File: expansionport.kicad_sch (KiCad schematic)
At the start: 23 parts

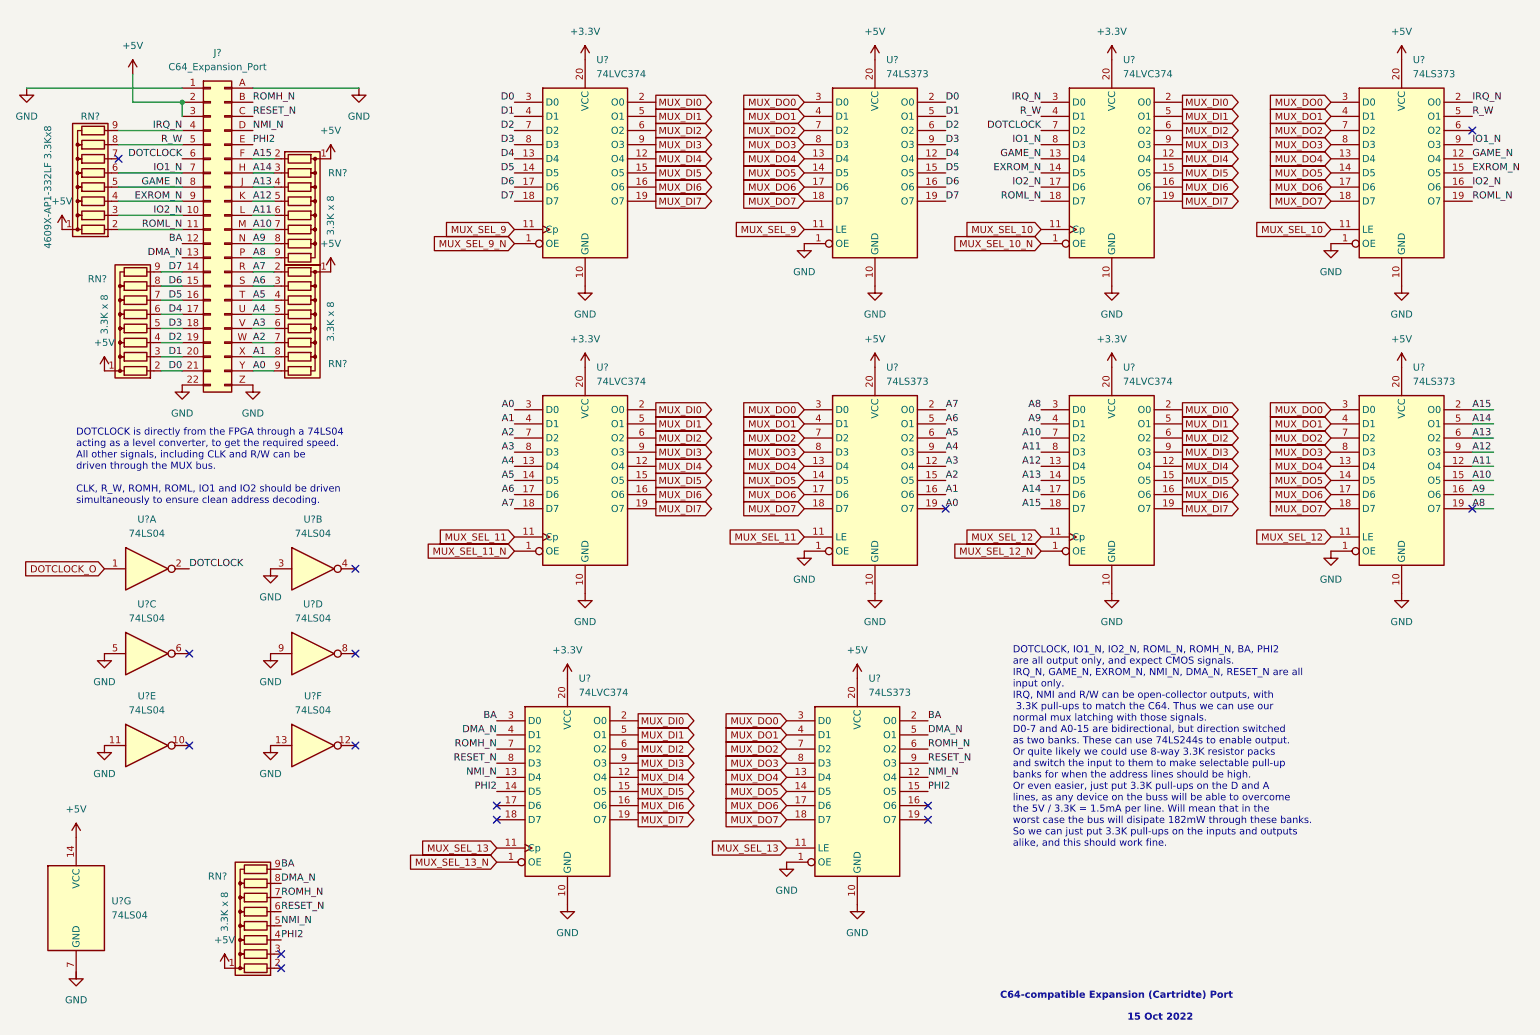
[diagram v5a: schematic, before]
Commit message: add all missing footprints
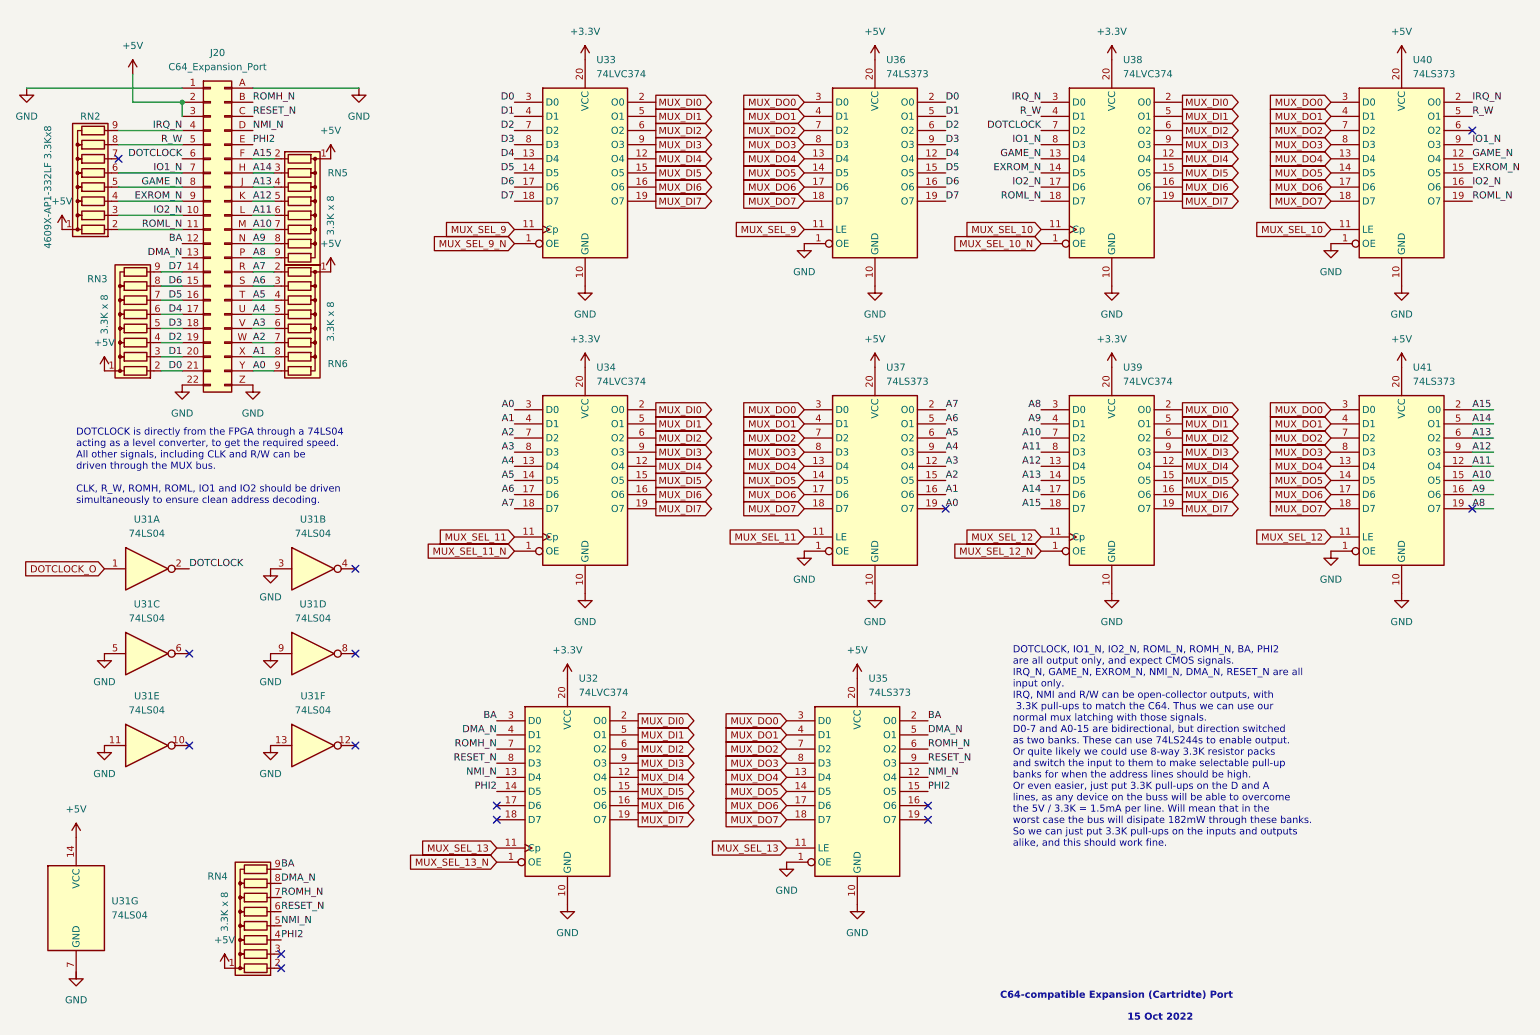
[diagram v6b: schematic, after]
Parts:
- U31: renamed from U?; footprint (none) -> Package_DIP:DIP-14_W7.62mm
- gave numbers to parts that had none: 16

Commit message: replace 74LS373s with 74LS374s #5
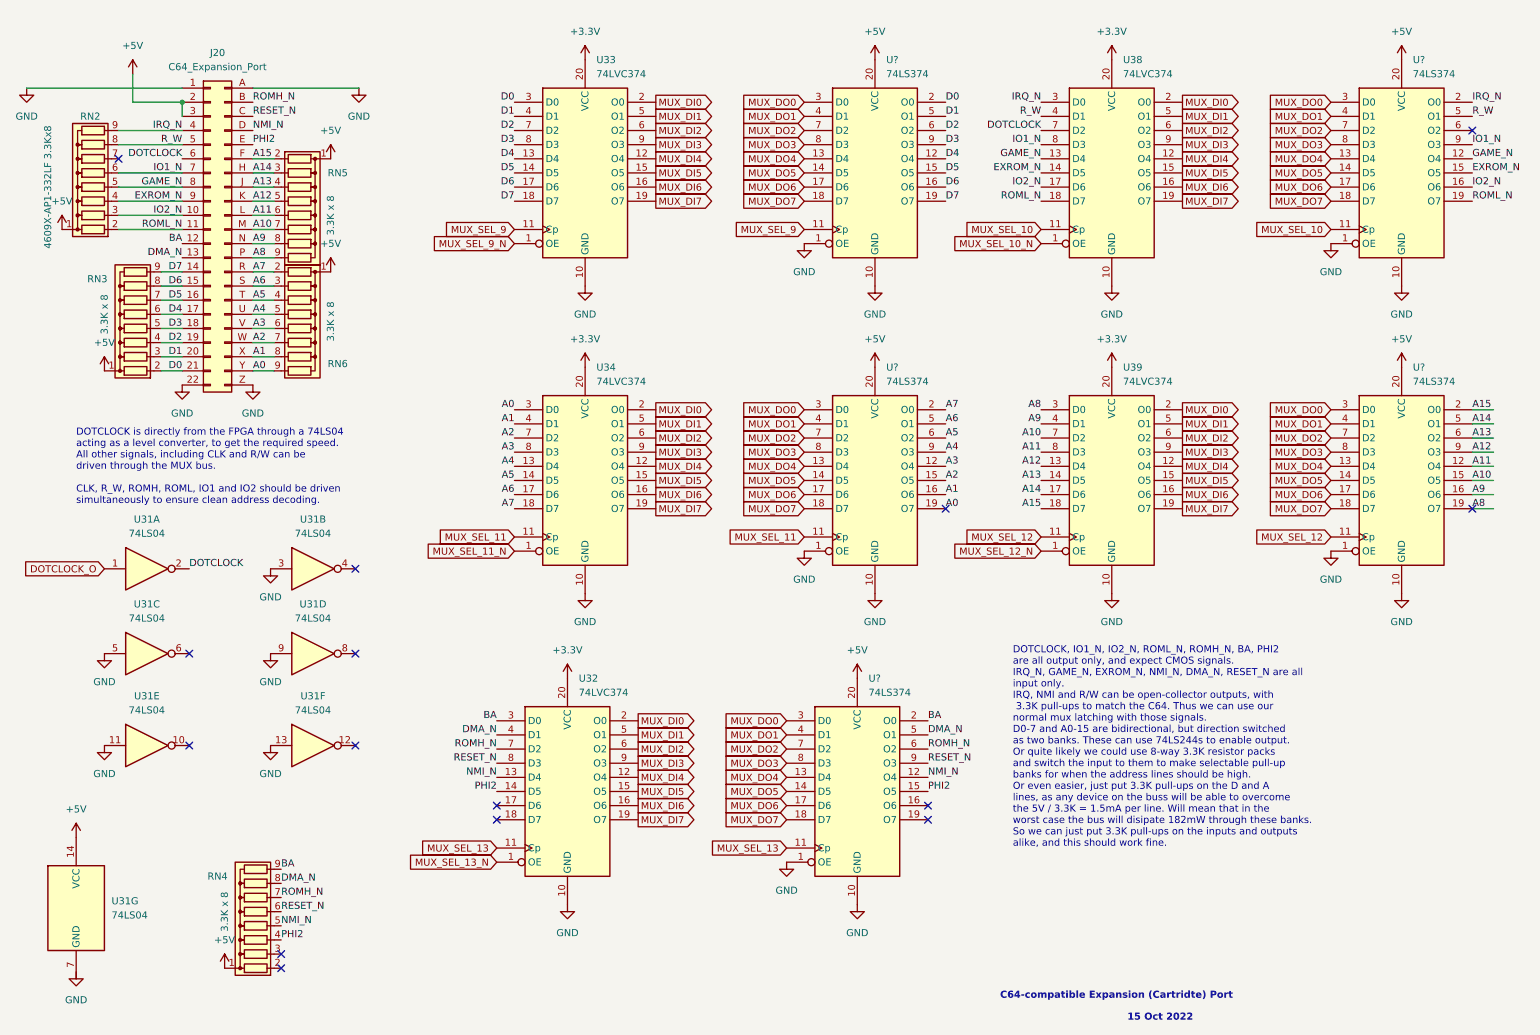
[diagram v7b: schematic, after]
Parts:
- removed U35, U36, U37, U40, U41: 74LS373, Package_DIP:DIP-20_W7.62mm, symbol 74xx:74LS373
- added U? (x5): 74LS374, Package_DIP:DIP-20_W7.62mm, symbol 74xx:74LS374
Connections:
- net +5V: now also U?.20 (VCC), U?.20 (VCC), U?.20 (VCC), U?.20 (VCC), U?.20 (VCC)
- net A0: now also U?.19 (O7)
- net A1: now also U?.16 (O6)
- net A10: now also U?.15 (O5)
- net A11: now also U?.12 (O4)
- net A12: now also U?.9 (O3)
- net A13: now also U?.6 (O2)
- net A14: now also U?.5 (O1)
- net A15: now also U?.2 (O0)
- net A2: now also U?.15 (O5)
- net A3: now also U?.12 (O4)
- net A4: now also U?.9 (O3)
- net A5: now also U?.6 (O2)
- net A6: now also U?.5 (O1)
- net A7: now also U?.2 (O0)
- net A8: now also U?.19 (O7)
- net A9: now also U?.16 (O6)
- net BA: now also U?.2 (O0)
- net D0: now also U?.2 (O0)
- net D1: now also U?.5 (O1)
- net D2: now also U?.6 (O2)
- net D3: now also U?.9 (O3)
- net D4: now also U?.12 (O4)
- net D5: now also U?.15 (O5)
- net D6: now also U?.16 (O6)
- net D7: now also U?.19 (O7)
- net DMA_N: now also U?.5 (O1)
- net EXROM_N: now also U?.15 (O5)
- net GAME_N: now also U?.12 (O4)
- net GND: now also U?.1 (OE), U?.1 (OE), U?.1 (OE), U?.1 (OE), U?.1 (OE), U?.10 (GND), U?.10 (GND), U?.10 (GND), U?.10 (GND), U?.10 (GND)
- net IO1_N: now also U?.9 (O3)
- net IO2_N: now also U?.16 (O6)
- net IRQ_N: now also U?.2 (O0)
- net MUX_DO0: now also U?.3 (D0), U?.3 (D0), U?.3 (D0), U?.3 (D0), U?.3 (D0)
- net MUX_DO1: now also U?.4 (D1), U?.4 (D1), U?.4 (D1), U?.4 (D1), U?.4 (D1)
- net MUX_DO2: now also U?.7 (D2), U?.7 (D2), U?.7 (D2), U?.7 (D2), U?.7 (D2)
- net MUX_DO3: now also U?.8 (D3), U?.8 (D3), U?.8 (D3), U?.8 (D3), U?.8 (D3)
- net MUX_DO4: now also U?.13 (D4), U?.13 (D4), U?.13 (D4), U?.13 (D4), U?.13 (D4)
- net MUX_DO5: now also U?.14 (D5), U?.14 (D5), U?.14 (D5), U?.14 (D5), U?.14 (D5)
- net MUX_DO6: now also U?.17 (D6), U?.17 (D6), U?.17 (D6), U?.17 (D6), U?.17 (D6)
- net MUX_DO7: now also U?.18 (D7), U?.18 (D7), U?.18 (D7), U?.18 (D7), U?.18 (D7)
- net MUX_SEL_10: now also U?.11 (Cp)
- net MUX_SEL_11: now also U?.11 (Cp)
- net MUX_SEL_12: now also U?.11 (Cp)
- net MUX_SEL_13: now also U?.11 (Cp)
- net MUX_SEL_9: now also U?.11 (Cp)
- net NMI_N: now also U?.12 (O4)
- net PHI2: now also U?.15 (O5)
- net RESET_N: now also U?.9 (O3)
- net ROMH_N: now also U?.6 (O2)
- net ROML_N: now also U?.19 (O7)
- net R_W: now also U?.5 (O1)

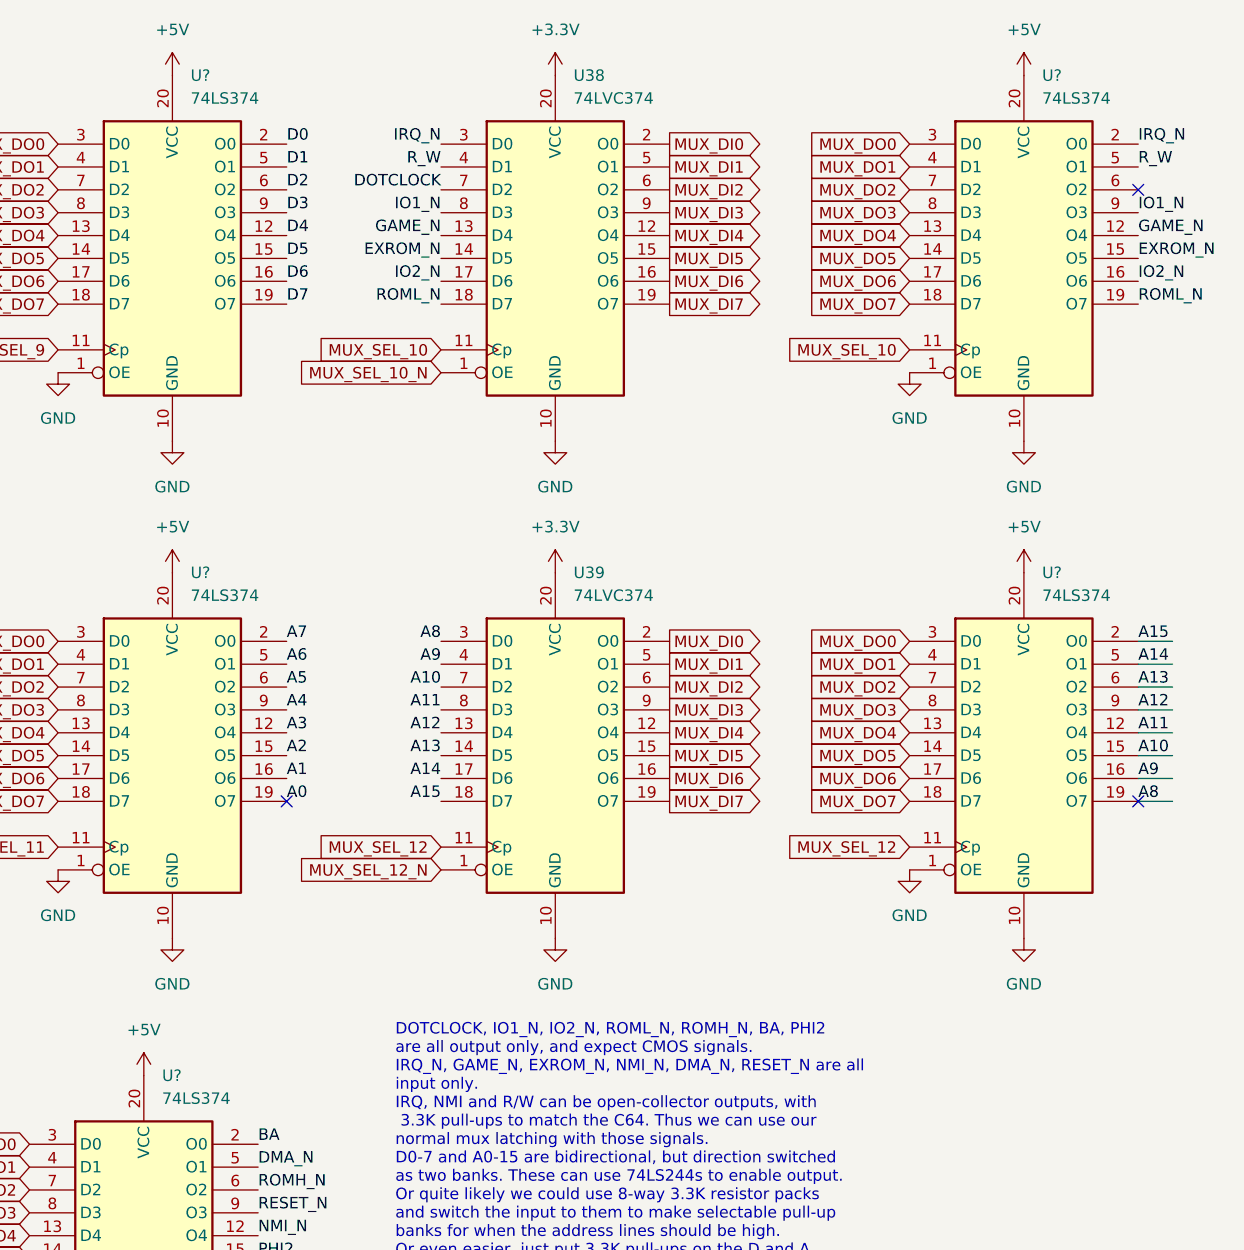
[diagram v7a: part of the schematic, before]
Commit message: replace remaining 74LS373 with 74LS374s #5
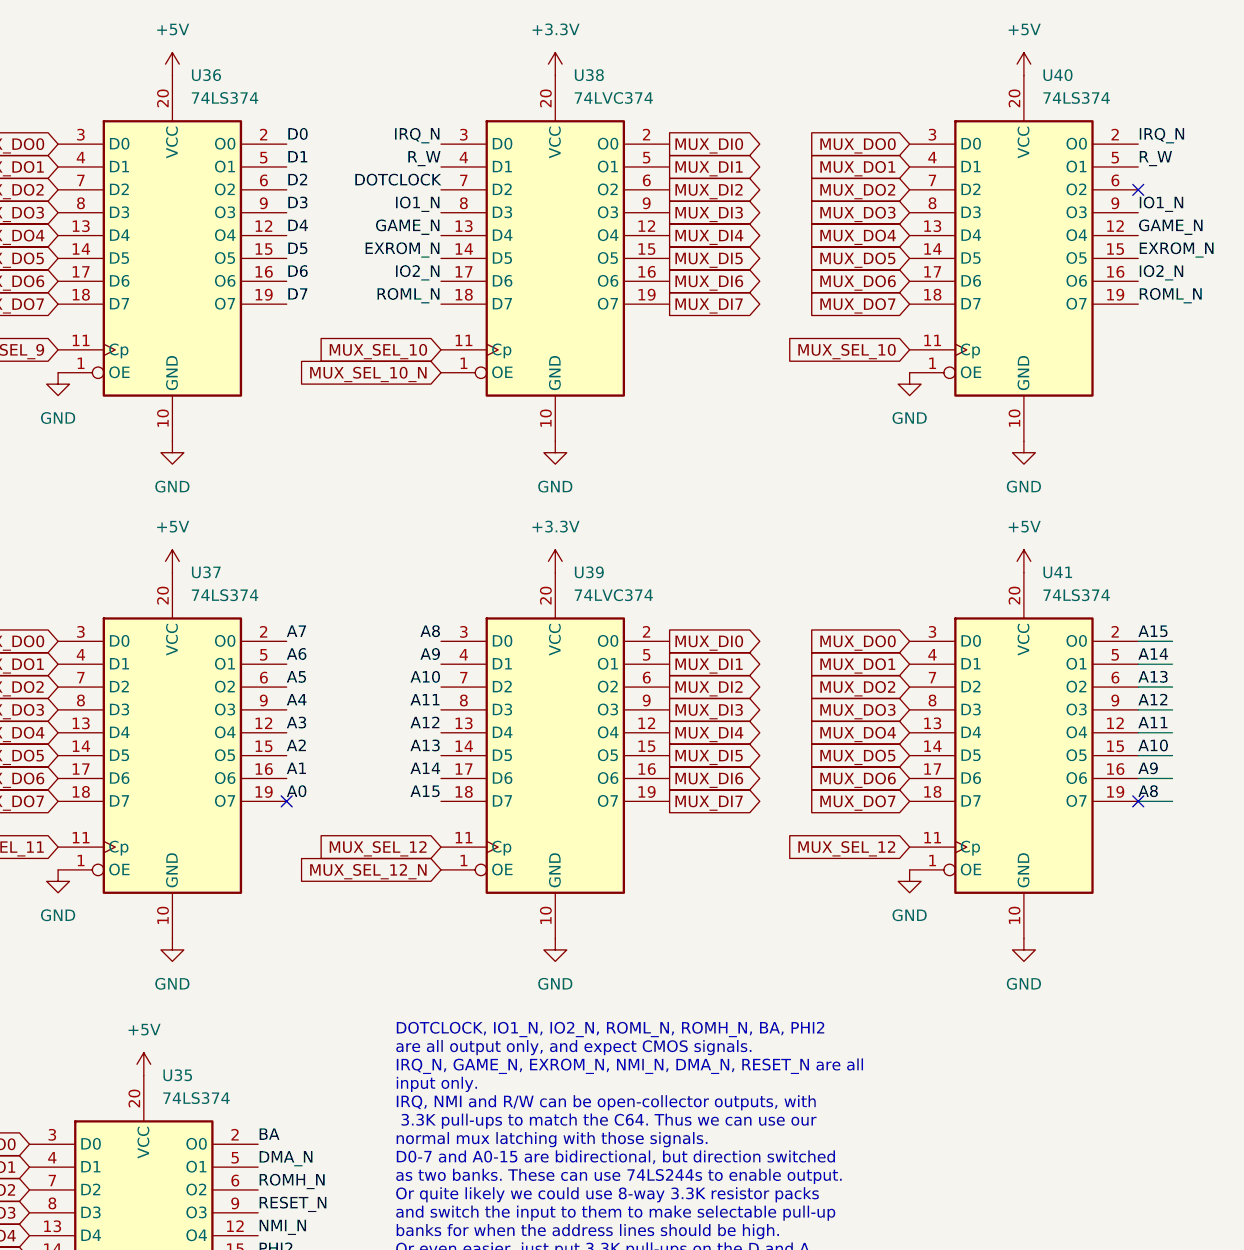
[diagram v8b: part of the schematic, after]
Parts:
- gave numbers to parts that had none: 5
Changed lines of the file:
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@@
   (symbol (lib_id "74xx:74LS374") (at 263.525 97.155 0) (unit 1)
     (in_bom yes) (on_board yes) (fields_autoplaced)
-    (property "Reference" "U?" (id 0) (at 265.5444 76.835 0)
+    (property "Reference" "U41" (id 0) (at 265.5444 76.835 0)
       (effects (font (size 1.27 1.27)) (justify left))
     )
@@
   (symbol (lib_id "74xx:74LS374") (at 263.525 41.91 0) (unit 1)
     (in_bom yes) (on_board yes) (fields_autoplaced)
-    (property "Reference" "U?" (id 0) (at 265.5444 21.59 0)
+    (property "Reference" "U40" (id 0) (at 265.5444 21.59 0)
       (effects (font (size 1.27 1.27)) (justify left))
     )
@@
   (symbol (lib_id "74xx:74LS374") (at 168.91 41.91 0) (unit 1)
     (in_bom yes) (on_board yes) (fields_autoplaced)
-    (property "Reference" "U?" (id 0) (at 170.9294 21.59 0)
+    (property "Reference" "U36" (id 0) (at 170.9294 21.59 0)
       (effects (font (size 1.27 1.27)) (justify left))
     )
@@
   (symbol (lib_id "74xx:74LS374") (at 165.735 153.035 0) (unit 1)
     (in_bom yes) (on_board yes) (fields_autoplaced)
-    (property "Reference" "U?" (id 0) (at 167.7544 132.715 0)
+    (property "Reference" "U35" (id 0) (at 167.7544 132.715 0)
       (effects (font (size 1.27 1.27)) (justify left))
     )
@@
   (symbol (lib_id "74xx:74LS374") (at 168.91 97.155 0) (unit 1)
     (in_bom yes) (on_board yes) (fields_autoplaced)
-    (property "Reference" "U?" (id 0) (at 170.9294 76.835 0)
-      (effects (font (size 1.27 1.27)) (justify left))
-    )
+    (property "Reference" "U37" (id 0) (at 170.9294 76.835 0)
+      (effects (font (size 1.27 1.27)) (justify left))
+    )
